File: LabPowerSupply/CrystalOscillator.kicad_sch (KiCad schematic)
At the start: 3 parts

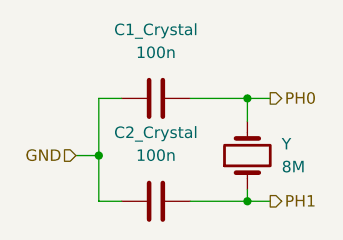
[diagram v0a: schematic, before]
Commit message: Finished first pass on the schematic
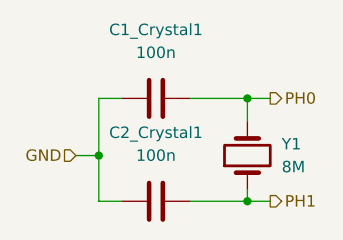
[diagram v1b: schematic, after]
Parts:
- renumbered C1_Crystal to C1_Crystal1, C2_Crystal to C2_Crystal1, Y to Y1
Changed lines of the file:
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@@
   (symbol (lib_id "Device:Crystal") (at 147.32 96.52 90) (unit 1)
     (in_bom yes) (on_board yes) (fields_autoplaced)
-    (property "Reference" "Y" (id 0) (at 151.13 95.2499 90)
+    (property "Reference" "Y1" (id 0) (at 151.13 95.2499 90)
       (effects (font (size 1.27 1.27)) (justify right))
     )
@@
   (symbol (lib_id "Device:C") (at 137.16 101.6 90) (unit 1)
     (in_bom yes) (on_board yes) (fields_autoplaced)
-    (property "Reference" "C2_Crystal" (id 0) (at 137.16 93.98 90))
+    (property "Reference" "C2_Crystal1" (id 0) (at 137.16 93.98 90))
     (property "Value" "100n" (id 1) (at 137.16 96.52 90))
     (property "Footprint" "Capacitor_SMD:C_1210_3225Metric" (id 2) (at 140.97 100.6348 0)
@@
   (symbol (lib_id "Device:C") (at 137.16 90.17 90) (unit 1)
     (in_bom yes) (on_board yes) (fields_autoplaced)
-    (property "Reference" "C1_Crystal" (id 0) (at 137.16 82.55 90))
+    (property "Reference" "C1_Crystal1" (id 0) (at 137.16 82.55 90))
     (property "Value" "100n" (id 1) (at 137.16 85.09 90))
     (property "Footprint" "Capacitor_SMD:C_1210_3225Metric" (id 2) (at 140.97 89.2048 0)
